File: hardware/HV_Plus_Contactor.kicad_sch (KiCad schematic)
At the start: 15 parts

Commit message: 🗿
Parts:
- removed C?: 1u, Capacitor_SMD:C_0603_1608Metric_Pad1.08x0.95mm_HandSolder, symbol Device:C
- removed C?: 0.1u, Capacitor_SMD:C_0603_1608Metric_Pad1.08x0.95mm_HandSolder, symbol Device:C
- removed D?: Contact, LED_SMD:LED_0603_1608Metric, symbol Device:LED
- removed D?: VSSAF522-M3/H, CustomKiCad-Library:SODFL5226X100N, symbol Diode:C3D25170H
- removed J?: ContactorConnector, UTSVT_Connectors:Molex_Nano-Fit_105309-xx04_1x04_P2.50mm_Vertical, symbol UTSVT_Connectors:ContactorConnector
- removed Q? (x2): IRLML0030, Package_TO_SOT_SMD:SOT-23, symbol Transistor_FET:IRLML0030
- removed R? (x4): 10k, symbol Device:R
- removed R?: 1k, symbol Device:R
- removed R?: 4.3k, symbol Device:R
- removed TP?: ctrl, TestPoint:TestPoint_Pad_1.0x1.0mm, symbol Connector:TestPoint
- removed TP?: Sense, TestPoint:TestPoint_Pad_1.0x1.0mm, symbol Connector:TestPoint
- added C?: 1u, Capacitor_SMD:C_0603_1608Metric_Pad1.08x0.95mm_HandSolder, symbol Device:C
- added C?: 0.1u, Capacitor_SMD:C_0603_1608Metric_Pad1.08x0.95mm_HandSolder, symbol Device:C
- added D?: VSSAF522-M3/H, CustomKiCad-Library:SODFL5226X100N, symbol Diode:C3D25170H
- added D?: Contact, LED_SMD:LED_0603_1608Metric, symbol Device:LED
- added J?: ContactorConnector, UTSVT_Connectors:Molex_Nano-Fit_105309-xx04_1x04_P2.50mm_Vertical, symbol UTSVT_Connectors:ContactorConnector
- added Q? (x2): IRLML0030, Package_TO_SOT_SMD:SOT-23, symbol Transistor_FET:IRLML0030
- added R?: 1k, symbol Device:R
- added R? (x4): 10k, symbol Device:R
- added R?: 4.3k, symbol Device:R
- added TP?: ctrl, TestPoint:TestPoint_Pad_1.0x1.0mm, symbol Connector:TestPoint
- added TP?: Sense, TestPoint:TestPoint_Pad_1.0x1.0mm, symbol Connector:TestPoint
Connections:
- net +24V: now also J?.1 (Con+(24V)), J?.4 (Sense+(24V))
- net 3.3V: now also Q?.3 (D)
- net CONTACTOR+: now also D?.1 (K), R?.2
- net CONTROL: now also Q?.1 (G), R?.2, TP?.1
- net GND: now also C?.1, C?.1, Q?.2 (S), R?.1, R?.1, R?.1
- net HV_CONTROL: now also D?.1 (K), D?.2 (A), J?.2 (Con-), Q?.3 (D)
- net SENSE: now also C?.2, Q?.2 (S), R?.2, TP?.1
- new net: R?.1, R?.1, R?.2
- new net: C?.2, Q?.1 (G), R?.2
- new net: J?.3 (Sense-), R?.2
- new net: D?.2 (A), R?.1

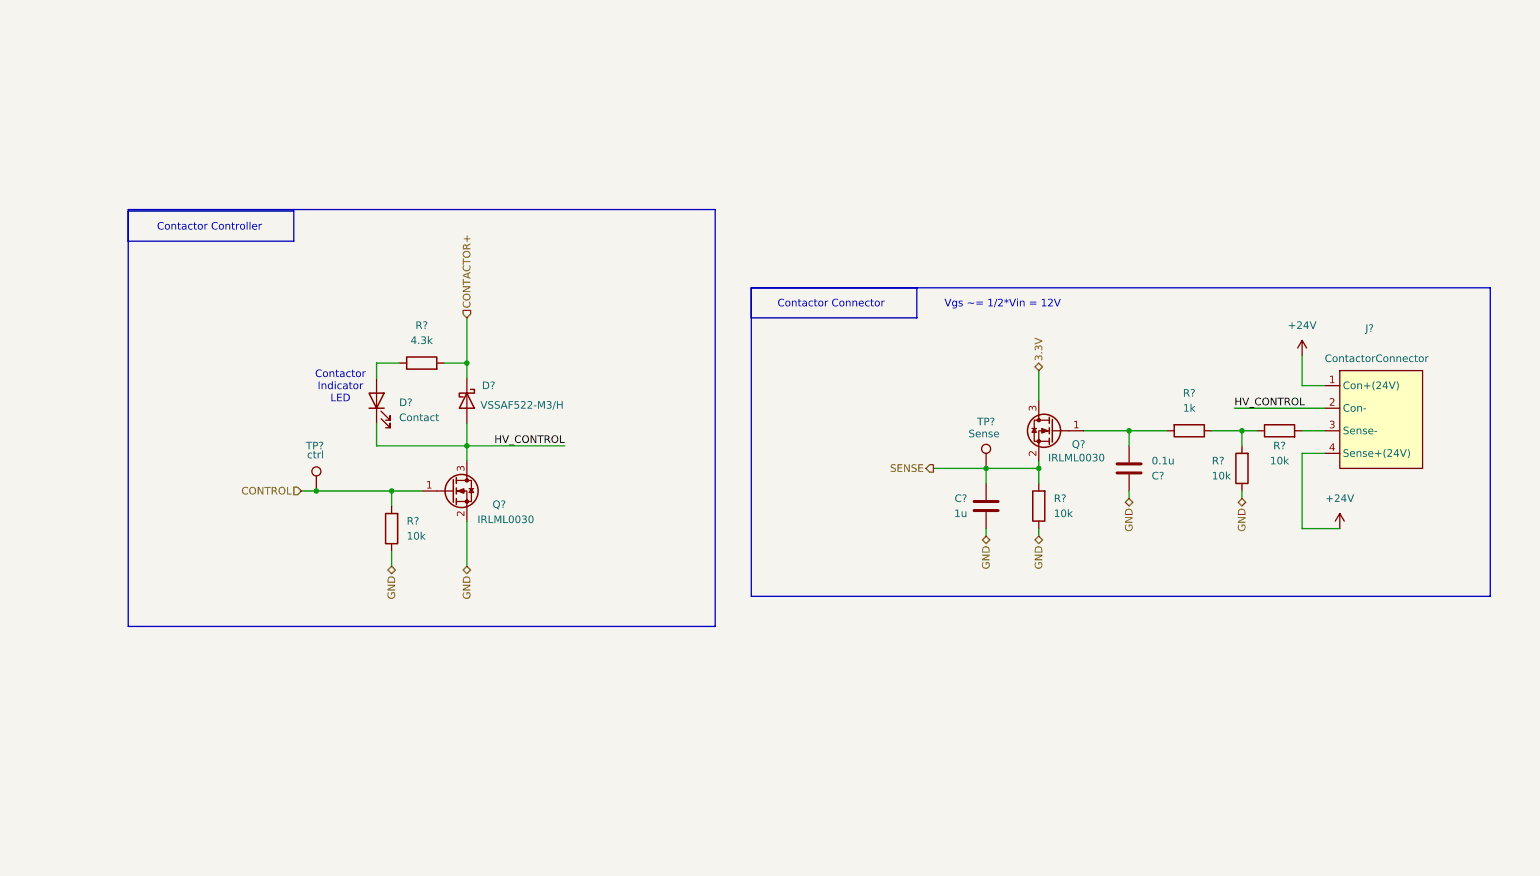
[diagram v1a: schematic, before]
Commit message: new contactor design block, started power mux
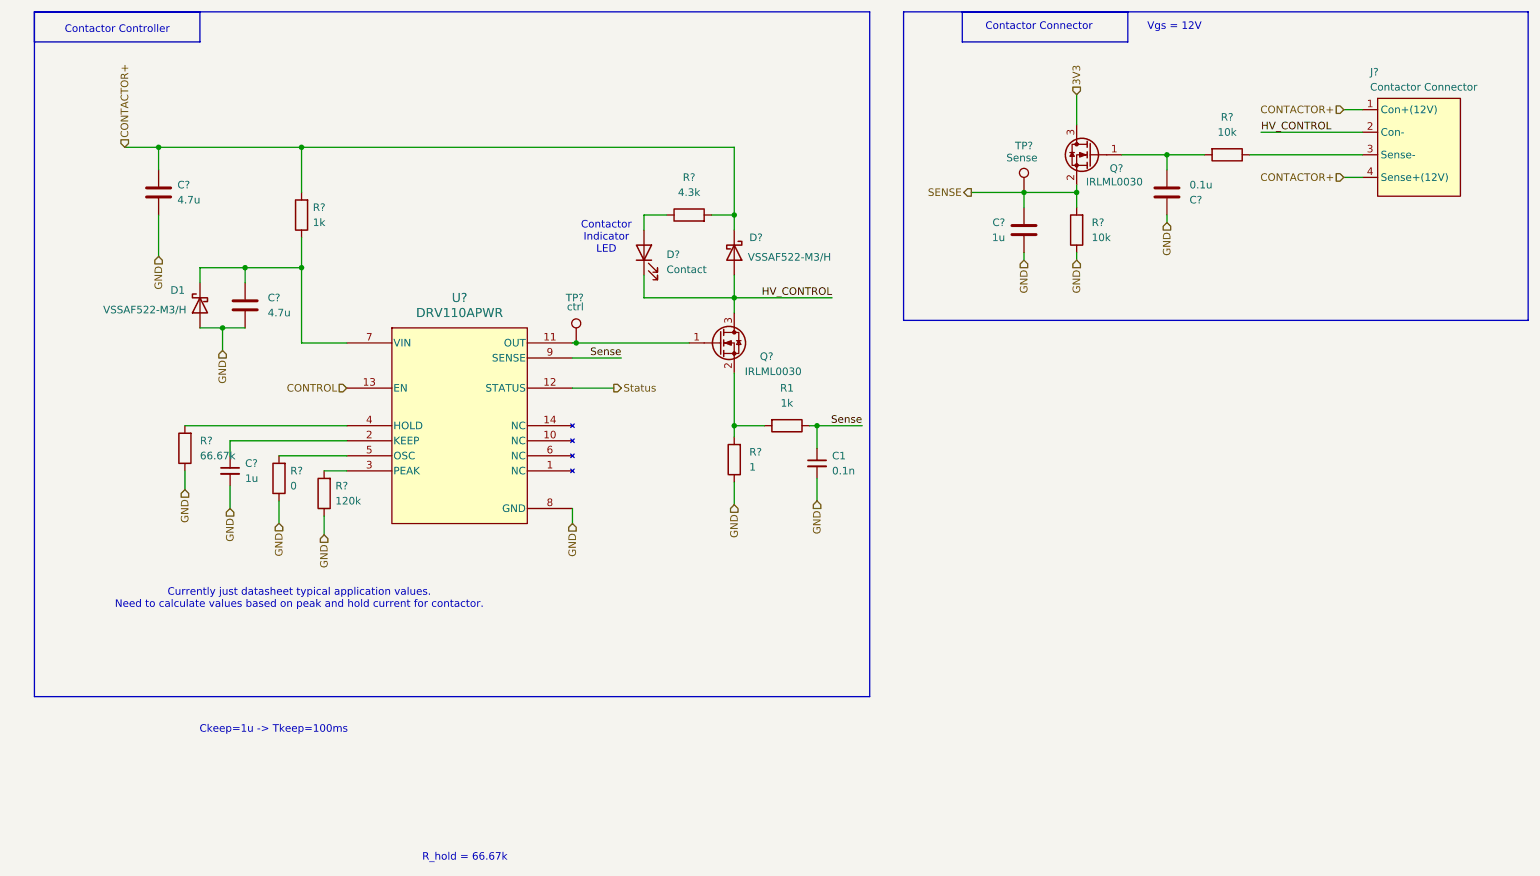
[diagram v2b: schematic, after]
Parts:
- removed C?: 1u, Capacitor_SMD:C_0603_1608Metric_Pad1.08x0.95mm_HandSolder, symbol Device:C
- removed C?: 0.1u, Capacitor_SMD:C_0603_1608Metric_Pad1.08x0.95mm_HandSolder, symbol Device:C
- removed D?: VSSAF522-M3/H, CustomKiCad-Library:SODFL5226X100N, symbol Diode:C3D25170H
- removed D?: Contact, LED_SMD:LED_0603_1608Metric, symbol Device:LED
- removed J?: ContactorConnector, UTSVT_Connectors:Molex_Nano-Fit_105309-xx04_1x04_P2.50mm_Vertical, symbol UTSVT_Connectors:ContactorConnector
- removed Q? (x2): IRLML0030, Package_TO_SOT_SMD:SOT-23, symbol Transistor_FET:IRLML0030
- removed R?: 1k, symbol Device:R
- removed R? (x4): 10k, symbol Device:R
- removed R?: 4.3k, symbol Device:R
- removed TP?: ctrl, TestPoint:TestPoint_Pad_1.0x1.0mm, symbol Connector:TestPoint
- removed TP?: Sense, TestPoint:TestPoint_Pad_1.0x1.0mm, symbol Connector:TestPoint
- added C1: 0.1n, symbol Device:C_Small
- added C? (x2): 4.7u, symbol Device:C
- added C?: 1u, Capacitor_SMD:C_0603_1608Metric_Pad1.08x0.95mm_HandSolder, symbol Device:C
- added C?: 0.1u, Capacitor_SMD:C_0603_1608Metric_Pad1.08x0.95mm_HandSolder, symbol Device:C
- added C?: 1u, symbol Device:C_Small
- added D1, D?: VSSAF522-M3/H, LHRS_Passives:SODFL5226X100N, symbol Diode:C3D25170H
- added D?: Contact, LED_SMD:LED_0603_1608Metric, symbol Device:LED
- added J?: Contactor Connector, LHRS_Connectors:Molex_Nano-Fit_105309-xx04_1x04_P2.50mm_Vertical, symbol lhrs_connectors:ContactorConnector
- added Q? (x2): IRLML0030, Package_TO_SOT_SMD:SOT-23, symbol Transistor_FET:IRLML0030
- added R1, R?: 1k, Resistor_SMD:R_0603_1608Metric_Pad0.98x0.95mm_HandSolder, symbol Device:R
- added R?: 120k, Resistor_SMD:R_0603_1608Metric_Pad0.98x0.95mm_HandSolder, symbol Device:R
- added R?: 0, Resistor_SMD:R_0603_1608Metric_Pad0.98x0.95mm_HandSolder, symbol Device:R
- added R? (x2): 10k, Resistor_SMD:R_0603_1608Metric_Pad0.98x0.95mm_HandSolder, symbol Device:R
- added R?: 66.67k, Resistor_SMD:R_0603_1608Metric_Pad0.98x0.95mm_HandSolder, symbol Device:R
- added R?: 1, Resistor_SMD:R_0603_1608Metric_Pad0.98x0.95mm_HandSolder, symbol Device:R
- added R?: 4.3k, Resistor_SMD:R_0603_1608Metric_Pad0.98x0.95mm_HandSolder, symbol Device:R
- added TP?: Sense, TestPoint:TestPoint_THTPad_D3.0mm_Drill1.5mm, symbol Connector:TestPoint
- added TP?: ctrl, TestPoint:TestPoint_THTPad_D3.0mm_Drill1.5mm, symbol Connector:TestPoint
- added U?: DRV110APWR, PW14_TEX, symbol lhrs_ics:DRV110APWR
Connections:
- net CONTACTOR+: now also C?.1, D?.1 (K), J?.1 (Con+(12V)), J?.4 (Sense+(12V)), R?.2, R?.2
- net CONTROL: now also U?.13 (EN)
- net GND: now also C1.2, C?.1, C?.1, C?.2, C?.2, C?.2, D1.2 (A), R?.1, R?.1, R?.1, R?.1, R?.1, U?.8 (GND)
- net HV_CONTROL: now also D?.1 (K), D?.2 (A), J?.2 (Con-), Q?.3 (D)
- net SENSE: now also C?.2, Q?.2 (S), R?.2, TP?.1
- new net: D?.2 (A), R?.1
- new net: C?.1, D1.1 (K), R?.1, U?.7 (VIN)
- new net: R?.2, U?.3 (PEAK)
- new net: R?.2, U?.5 (OSC)
- new net: Q?.1 (G), TP?.1, U?.11 (OUT)
- new net: C?.1, U?.2 (KEEP)
- new net: R?.2, U?.4 (HOLD)
- new net: J?.3 (Sense-), R?.1
- new net: C?.2, Q?.1 (G), R?.2
- new net: Q?.2 (S), R1.2, R?.2
- new net 3V3: Q?.3 (D)
- new net Sense: C1.1, R1.1, U?.9 (SENSE)
- new net Status: U?.12 (STATUS)
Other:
- note added: "Ckeep=1u -> Tkeep=100ms"
- note added: "Currently just datasheet typical application values. Need to calculate values based on peak and hold current for contactor."
- note added: "R_hold = 66.67k"
- note added: "Vgs = 12V"
- note removed: "Vgs ~= 1/2*Vin = 12V"

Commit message: finished schematic except for 12v buck boost
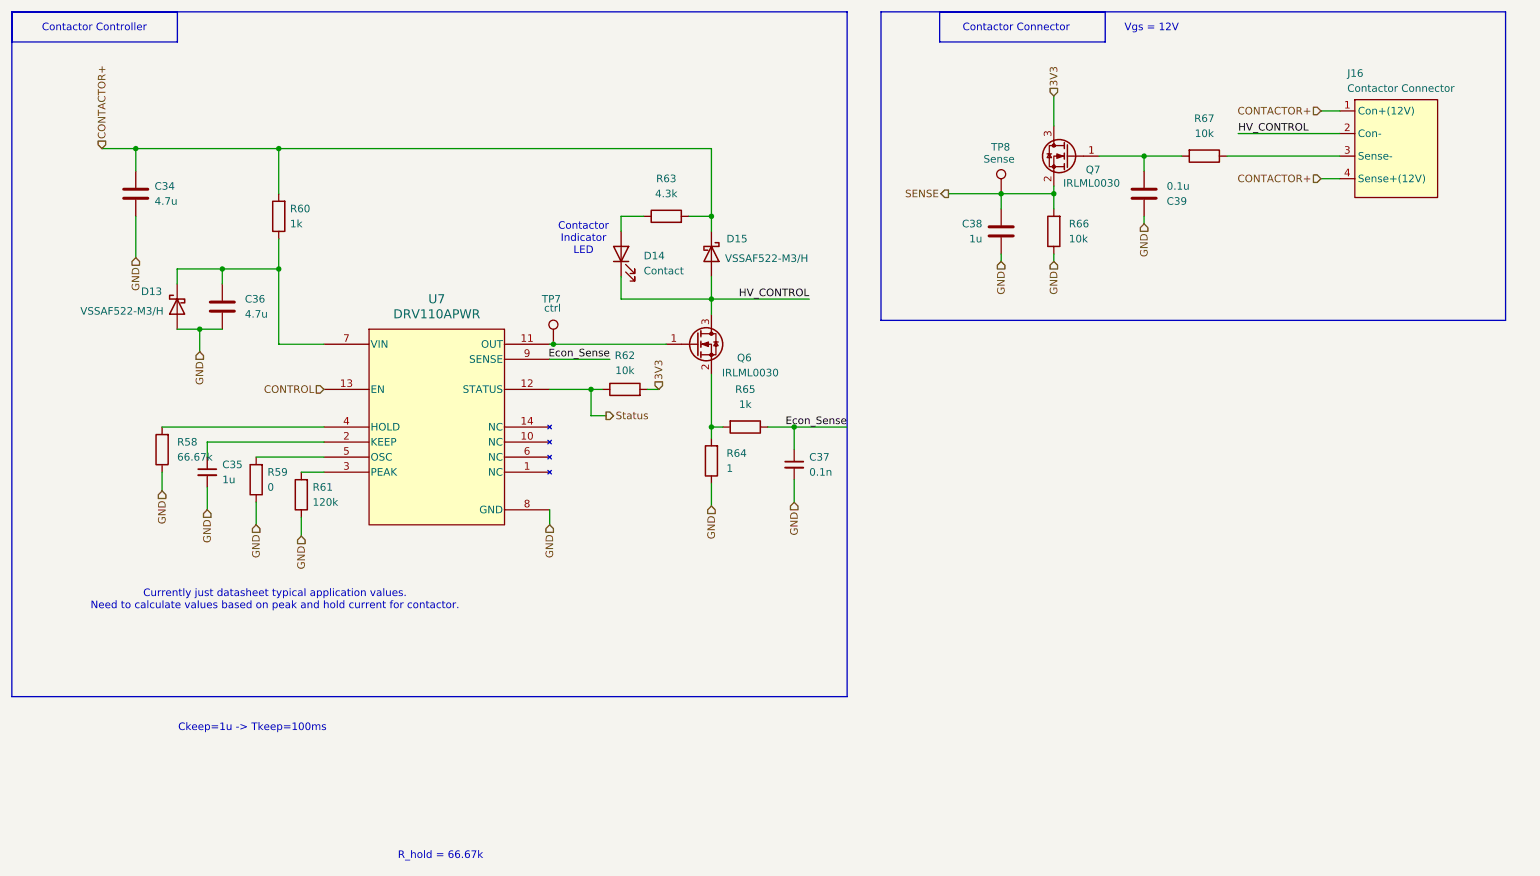
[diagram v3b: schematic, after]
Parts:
- removed C1: 0.1n, symbol Device:C_Small
- removed C? (x2): 4.7u, symbol Device:C
- removed C?: 1u, Capacitor_SMD:C_0603_1608Metric_Pad1.08x0.95mm_HandSolder, symbol Device:C
- removed C?: 0.1u, Capacitor_SMD:C_0603_1608Metric_Pad1.08x0.95mm_HandSolder, symbol Device:C
- removed C?: 1u, symbol Device:C_Small
- removed D1, D?: VSSAF522-M3/H, LHRS_Passives:SODFL5226X100N, symbol Diode:C3D25170H
- removed D?: Contact, LED_SMD:LED_0603_1608Metric, symbol Device:LED
- removed J?: Contactor Connector, LHRS_Connectors:Molex_Nano-Fit_105309-xx04_1x04_P2.50mm_Vertical, symbol lhrs_connectors:ContactorConnector
- removed Q? (x2): IRLML0030, Package_TO_SOT_SMD:SOT-23, symbol Transistor_FET:IRLML0030
- removed R1, R?: 1k, Resistor_SMD:R_0603_1608Metric_Pad0.98x0.95mm_HandSolder, symbol Device:R
- removed R?: 120k, Resistor_SMD:R_0603_1608Metric_Pad0.98x0.95mm_HandSolder, symbol Device:R
- removed R?: 0, Resistor_SMD:R_0603_1608Metric_Pad0.98x0.95mm_HandSolder, symbol Device:R
- removed R? (x2): 10k, Resistor_SMD:R_0603_1608Metric_Pad0.98x0.95mm_HandSolder, symbol Device:R
- removed R?: 66.67k, Resistor_SMD:R_0603_1608Metric_Pad0.98x0.95mm_HandSolder, symbol Device:R
- removed R?: 1, Resistor_SMD:R_0603_1608Metric_Pad0.98x0.95mm_HandSolder, symbol Device:R
- removed R?: 4.3k, Resistor_SMD:R_0603_1608Metric_Pad0.98x0.95mm_HandSolder, symbol Device:R
- removed TP?: Sense, TestPoint:TestPoint_THTPad_D3.0mm_Drill1.5mm, symbol Connector:TestPoint
- removed TP?: ctrl, TestPoint:TestPoint_THTPad_D3.0mm_Drill1.5mm, symbol Connector:TestPoint
- removed U?: DRV110APWR, PW14_TEX, symbol lhrs_ics:DRV110APWR
- added C34, C36: 4.7u, Capacitor_SMD:C_0805_2012Metric_Pad1.18x1.45mm_HandSolder, symbol Device:C
- added C35: 1u, Capacitor_SMD:C_0603_1608Metric_Pad1.08x0.95mm_HandSolder, symbol Device:C_Small
- added C37: 0.1n, Capacitor_SMD:C_0603_1608Metric_Pad1.08x0.95mm_HandSolder, symbol Device:C_Small
- added C38: 1u, Capacitor_SMD:C_0603_1608Metric_Pad1.08x0.95mm_HandSolder, symbol Device:C
- added C39: 0.1u, Capacitor_SMD:C_0603_1608Metric_Pad1.08x0.95mm_HandSolder, symbol Device:C
- added D13, D15: VSSAF522-M3/H, LHRS_Passives:SODFL5226X100N, symbol Diode:C3D25170H
- added D14: Contact, LED_SMD:LED_0603_1608Metric_Pad1.05x0.95mm_HandSolder, symbol Device:LED
- added J16: Contactor Connector, LHRS_Connectors:Molex_Nano-Fit_105309-xx04_1x04_P2.50mm_Vertical, symbol lhrs_connectors:ContactorConnector
- added Q6, Q7: IRLML0030, Package_TO_SOT_SMD:SOT-23, symbol Transistor_FET:IRLML0030
- added R58: 66.67k, Resistor_SMD:R_0603_1608Metric_Pad0.98x0.95mm_HandSolder, symbol Device:R
- added R59: 0, Resistor_SMD:R_0603_1608Metric_Pad0.98x0.95mm_HandSolder, symbol Device:R
- added R60, R65: 1k, Resistor_SMD:R_0603_1608Metric_Pad0.98x0.95mm_HandSolder, symbol Device:R
- added R61: 120k, Resistor_SMD:R_0603_1608Metric_Pad0.98x0.95mm_HandSolder, symbol Device:R
- added R62, R66, R67: 10k, Resistor_SMD:R_0603_1608Metric_Pad0.98x0.95mm_HandSolder, symbol Device:R
- added R63: 4.3k, Resistor_SMD:R_0603_1608Metric_Pad0.98x0.95mm_HandSolder, symbol Device:R
- added R64: 1, Resistor_SMD:R_0603_1608Metric_Pad0.98x0.95mm_HandSolder, symbol Device:R
- added TP7: ctrl, TestPoint:TestPoint_THTPad_D3.0mm_Drill1.5mm, symbol Connector:TestPoint
- added TP8: Sense, TestPoint:TestPoint_THTPad_D3.0mm_Drill1.5mm, symbol Connector:TestPoint
- added U7: DRV110APWR, LHRS_ICs:PW14_TEX, symbol lhrs_ics:DRV110APWR
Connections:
- net 3V3: now also Q7.3 (D), R62.2
- net CONTACTOR+: now also C34.1, D15.1 (K), J16.1 (Con+(12V)), J16.4 (Sense+(12V)), R60.2, R63.2
- net CONTROL: now also U7.13 (EN)
- net GND: now also C34.2, C35.2, C36.2, C37.2, C38.1, C39.1, D13.2 (A), R58.1, R59.1, R61.1, R64.1, R66.1, U7.8 (GND)
- net HV_CONTROL: now also D14.1 (K), D15.2 (A), J16.2 (Con-), Q6.3 (D)
- net SENSE: now also C38.2, Q7.2 (S), R66.2, TP8.1
- net Status: now also R62.1, U7.12 (STATUS)
- new net: R58.2, U7.4 (HOLD)
- new net: D14.2 (A), R63.1
- new net: C36.1, D13.1 (K), R60.1, U7.7 (VIN)
- new net: Q6.1 (G), TP7.1, U7.11 (OUT)
- new net: Q6.2 (S), R64.2, R65.2
- new net: C35.1, U7.2 (KEEP)
- new net: R59.2, U7.5 (OSC)
- new net: R61.2, U7.3 (PEAK)
- new net: C39.2, Q7.1 (G), R67.2
- new net: J16.3 (Sense-), R67.1
- new net Econ_Sense: C37.1, R65.1, U7.9 (SENSE)
